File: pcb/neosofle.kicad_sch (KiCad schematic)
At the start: 69 parts, among them J1 JST_01x02_Socket, J2 JST_01x02_Pin, SW1 CPG135001S30, SW10 CPG135001S30, SW11 CPG135001S30, SW12 CPG135001S30, SW13 CPG135001S30, SW14 CPG135001S30, SW15 CPG135001S30, SW16 CPG135001S30, SW17 CPG135001S30, SW18 CPG135001S30, SW19 CPG135001S30, SW2 CPG135001S30, SW20 CPG135001S30, SW21 CPG135001S30, SW22 CPG135001S30, SW23 CPG135001S30, SW24 CPG135001S30, SW25 RotaryEncoder_Switch, SW26 CPG135001S30, SW27 CPG135001S30, SW28 CPG135001S30, SW29 CPG135001S30, SW3 CPG135001S30, SW30 CPG135001S30, SW4 CPG135001S30, SW5 CPG135001S30, SW6 CPG135001S30, SW7 CPG135001S30, SW8 CPG135001S30, SW9 CPG135001S30, U1 nice!nano v2

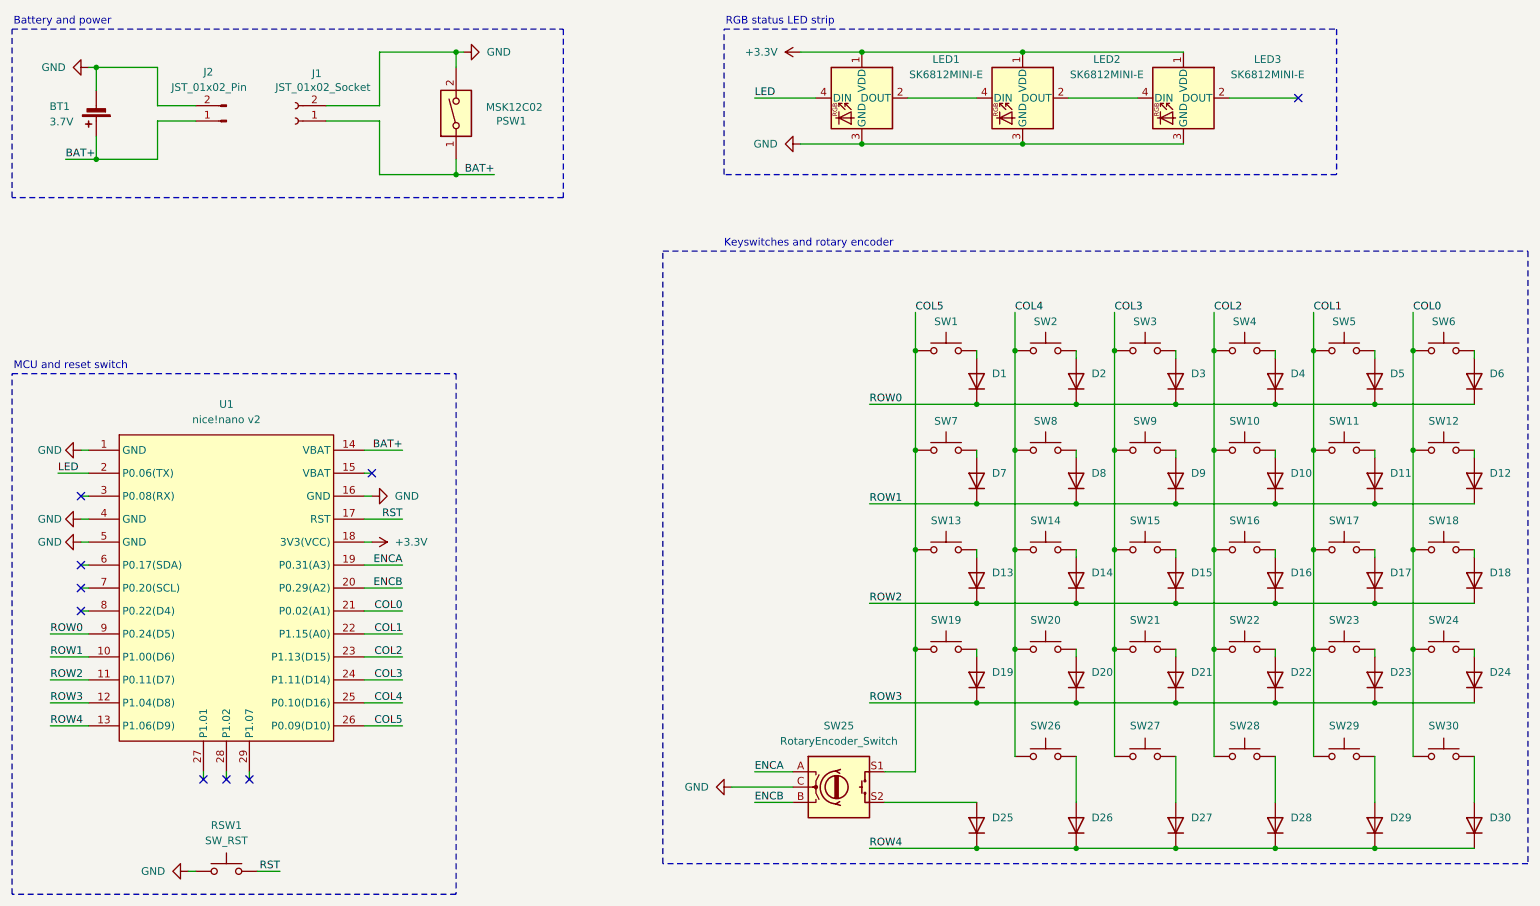
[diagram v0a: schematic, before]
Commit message: Correct battery and power net and their labels.
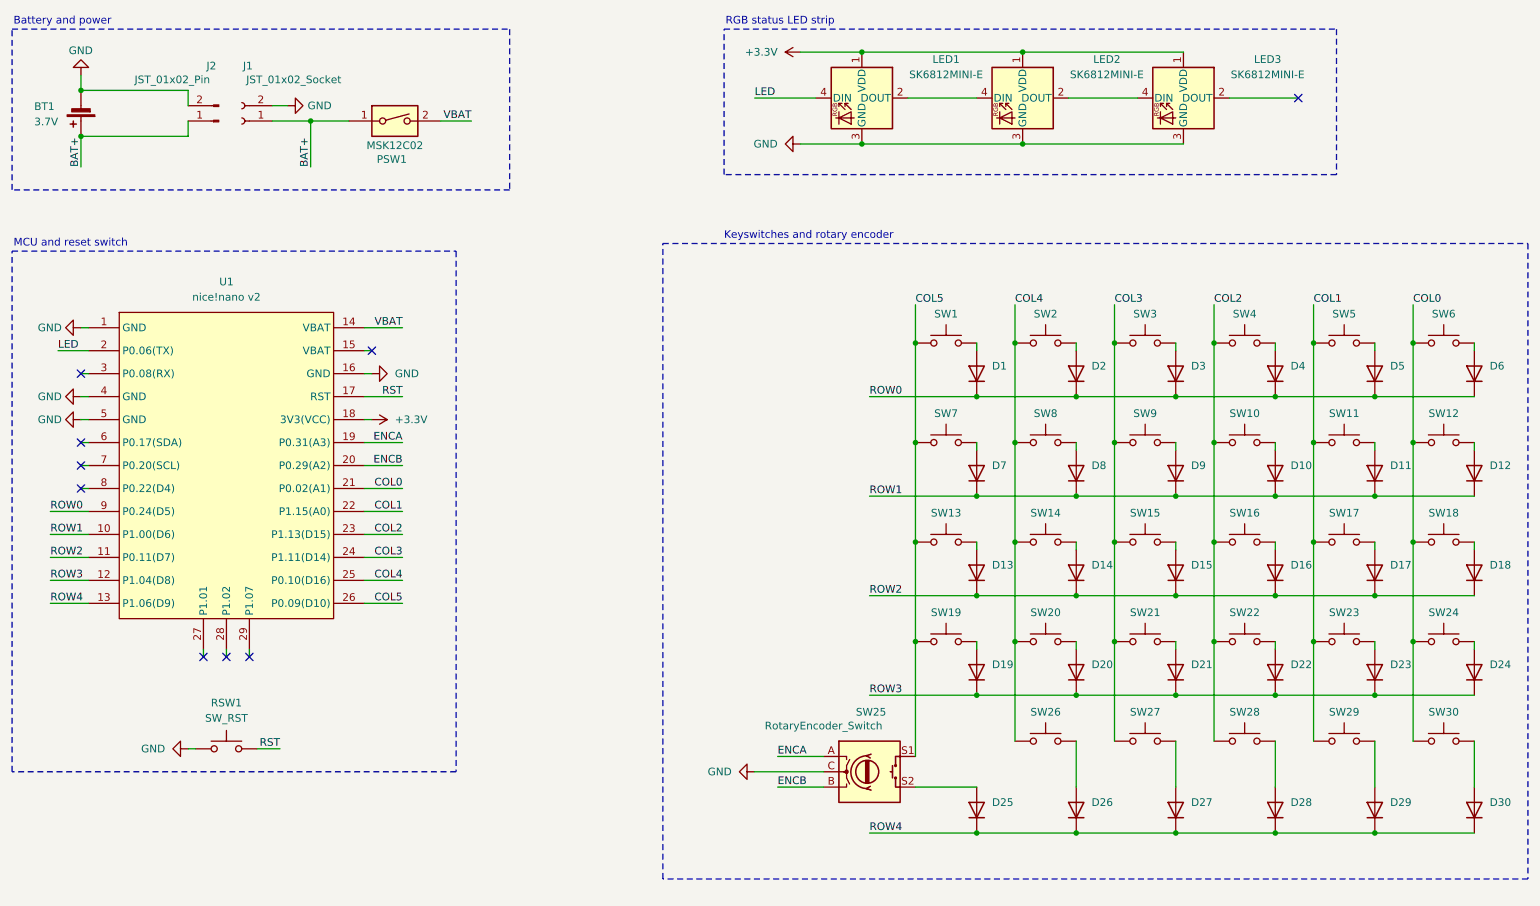
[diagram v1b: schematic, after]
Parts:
- LED1, LED2, LED3: footprint neosofle:SK6812MINI-E -> Custom_Keyboard:LED_SK6812MINI-E
- PSW1: footprint Custom_Keyboard:SW_Slide_SPDT_MSK12C02_HandSolder_Reversible -> Button_Switch_SMD:SW_SPDT_Shouhan_MSK12C02
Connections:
- net BAT+: no longer U1.14 (VBAT)
- net GND: no longer PSW1.2
- new net VBAT: PSW1.2, U1.14 (VBAT)
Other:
- moved on the sheet: BT1, D1, D10, D11, D12, D13, D14, D15, D16, D17, D18, D19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

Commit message: Add footprints, rename project to NeoSofle.
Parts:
- D1, D10, D11, D12, D13, D14, D15, D16, D17, D18, D19, D2, D20, D21, D22, D23, D24, D25, D26, D27, D28, D29, D3, D30, D4, D5, D6, D7, D8, D9: footprint Custom_Keyboard:D_SOD-123F_HandSolder_Reversible -> NeoSofle:D_SOD-123F_HandSolder
- J1: value JST_01x02_Socket -> JST_ACH_BM02B-ACHSS-GAN-ETF_Socket; footprint Custom_Keyboard:JST_ACH_BM02B-ACHSS-GAN-ETF_1x02-1MP_P1.20mm_Vertical_Reversible -> NeoSofle:JST_ACH_BM02B-ACHSS-GAN-ETF_1x02-1MP_P1.20mm_Vertical_HandSolder_Reversible
- J2: value JST_01x02_Pin -> JST_ACH_BM02B-ACHSS-GAN-ETF_Pin
- LED1, LED2, LED3: footprint Custom_Keyboard:LED_SK6812MINI-E -> NeoSofle:LED_SK6812MINI-E; symbol neosofle:SK6812MINI-E -> NeoSofle:SK6812MINI-E
- PSW1: footprint Button_Switch_SMD:SW_SPDT_Shouhan_MSK12C02 -> NeoSofle:SW_SPDT_MSK12C02_HandSolder
- RSW1: footprint Custom_Keyboard:SW_PUSH_1P1T_6x3.5mm_H4.3_APEM_MJTP1243_Reversible -> Button_Switch_THT:SW_PUSH_1P1T_6x3.5mm_H4.3_APEM_MJTP1243
- SW1, SW10, SW11, SW12, SW13, SW14, SW15, SW16, SW17, SW18, SW19, SW2, SW20, SW21, SW22, SW23, SW24, SW26, SW27, SW28, SW29, SW3, SW30, SW4, SW5, SW6, SW7, SW8, SW9: footprint Custom_Keyboard:SW_Choc_V2_HS_CPG135001S30_1u_Reversible -> NeoSofle:SW_Choc_V2_HS_CPG135001S30_1u
- SW25: footprint Custom_Keyboard:RotaryEncoder_Alps_EC11E-Switch_Vertical_H20mm_Reversible -> NeoSofle:RotaryEncoder_Bourns_PEC11L-Switch_Vertical15mm
- U1: footprint neosofle:nice_nano_Reversible -> NeoSofle:Nice_Nano_V2; symbol neosofle:nice_nano -> NeoSofle:nice_nano; now in the parts list

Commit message: Add 1u / 1.5u hybrid footprint for thumbkey, add teardrops, round tracks, add logo art and version text.
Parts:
- SW26: footprint NeoSofle:SW_Choc_V2_HS_CPG135001S30_1u -> NeoSofle:SW_Choc_V2_HS_CPG135001S30_1u1.5u_Hybrid
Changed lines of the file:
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@@
 			)
 		)
-		(property "Footprint" "NeoSofle:SW_Choc_V2_HS_CPG135001S30_1u"
+		(property "Footprint" "NeoSofle:SW_Choc_V2_HS_CPG135001S30_1u1.5u_Hybrid"
 			(at 194.31 132.08 0)
 			(effects

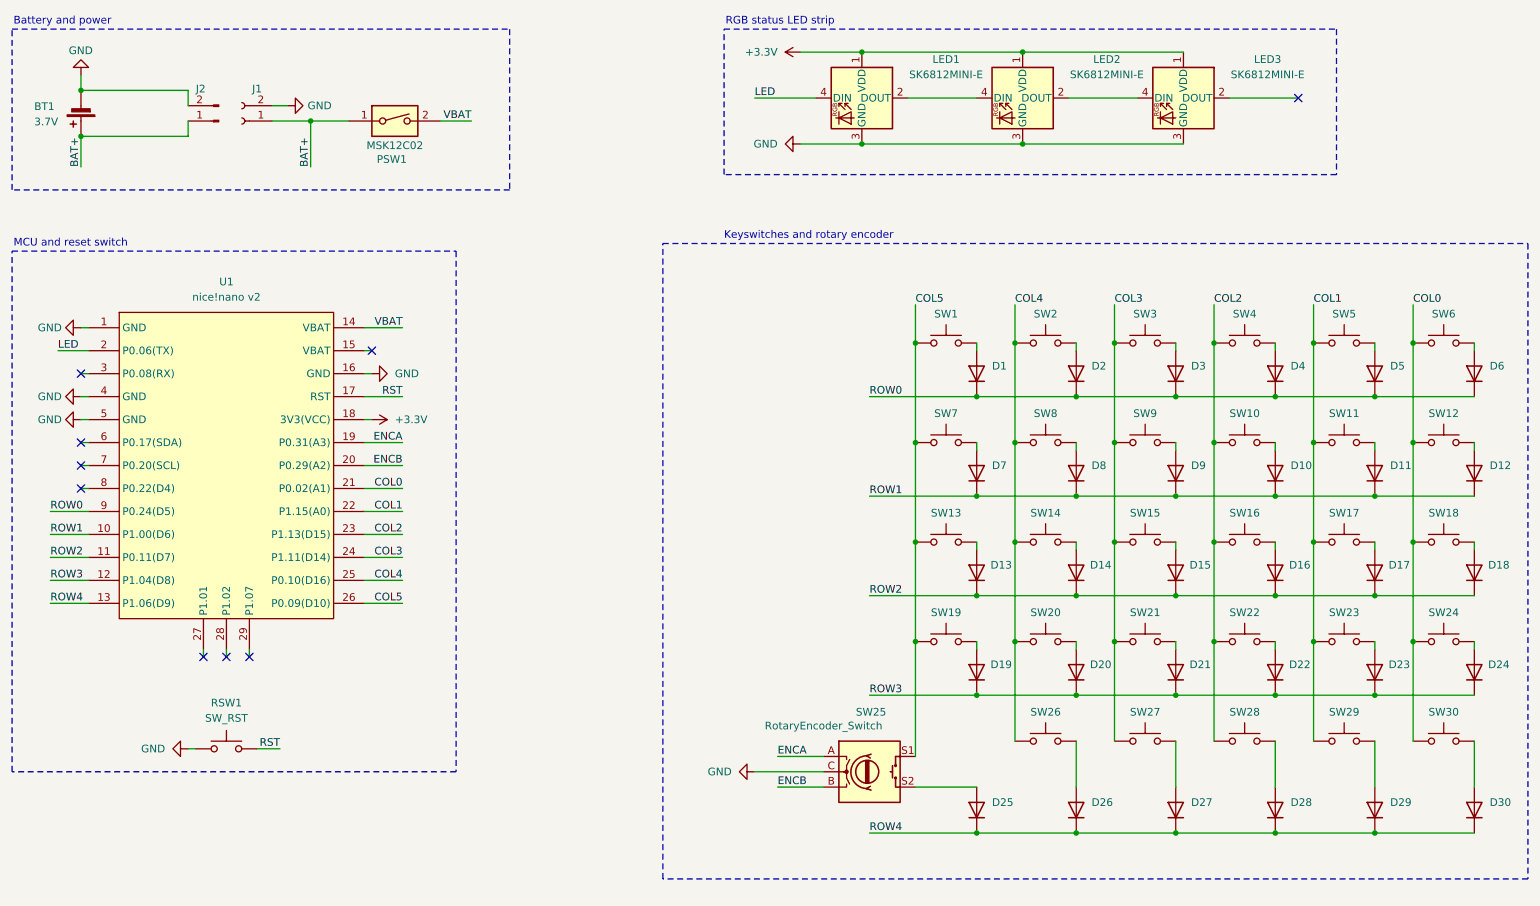
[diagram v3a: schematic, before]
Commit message: Update to hierarchical schematic reuse for both left and right half.
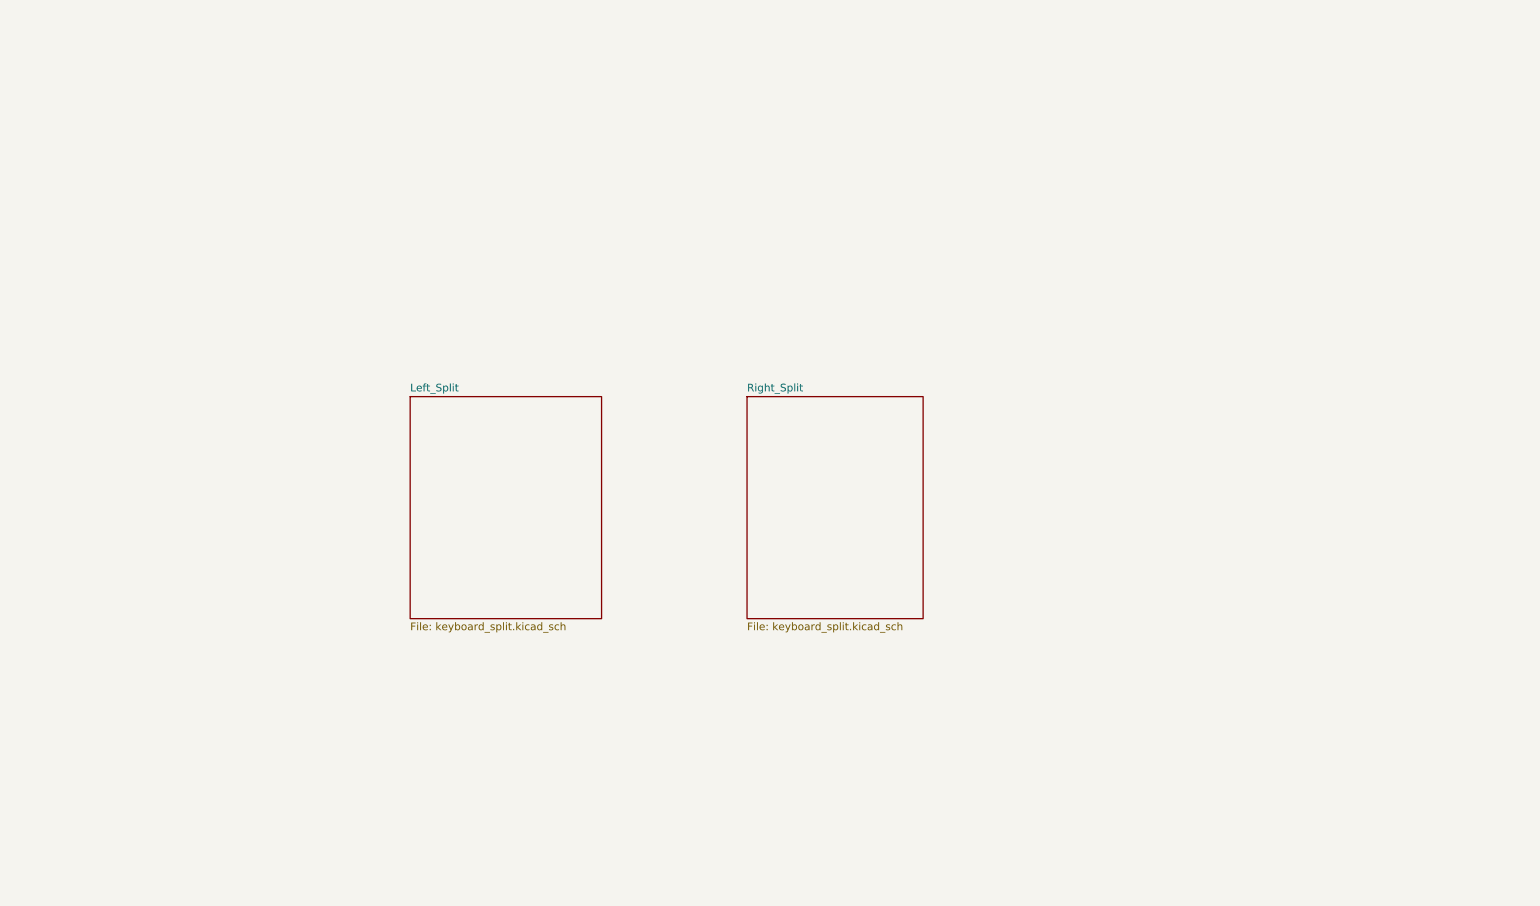
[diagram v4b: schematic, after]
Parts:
- removed BT1: 3.7V, symbol Device:Battery_Cell
- removed D1, D10, D11, D12, D13, D14, D15, D16, D17, D18, D19, D2, D20, D21, D22, D23, D24, D25, D26, D27, D28, D29, D3, D30, D4, D5, D6, D7, D8, D9: 1N4148W, NeoSofle:D_SOD-123F_HandSolder, symbol Diode:1N4148W
- removed J1: JST_ACH_BM02B-ACHSS-GAN-ETF_Socket, NeoSofle:JST_ACH_BM02B-ACHSS-GAN-ETF_1x02-1MP_P1.20mm_Vertical_HandSolder_Reversible, symbol Connector:Conn_01x02_Socket
- removed J2: JST_ACH_BM02B-ACHSS-GAN-ETF_Pin, symbol Connector:Conn_01x02_Pin
- removed LED1, LED2, LED3: SK6812MINI-E, NeoSofle:LED_SK6812MINI-E, symbol NeoSofle:SK6812MINI-E
- removed PSW1: MSK12C02, NeoSofle:SW_SPDT_MSK12C02_HandSolder, symbol Switch:SW_DIP_x01
- removed RSW1: SW_RST, Button_Switch_THT:SW_PUSH_1P1T_6x3.5mm_H4.3_APEM_MJTP1243, symbol Switch:SW_Push
- removed SW1, SW10, SW11, SW12, SW13, SW14, SW15, SW16, SW17, SW18, SW19, SW2, SW20, SW21, SW22, SW23, SW24, SW27, SW28, SW29, SW3, SW30, SW4, SW5, SW6, SW7, SW8, SW9: CPG135001S30, NeoSofle:SW_Choc_V2_HS_CPG135001S30_1u, symbol Switch:SW_Push
- removed SW25: RotaryEncoder_Switch, NeoSofle:RotaryEncoder_Bourns_PEC11L-Switch_Vertical15mm, symbol Device:RotaryEncoder_Switch
- removed SW26: CPG135001S30, NeoSofle:SW_Choc_V2_HS_CPG135001S30_1u1.5u_Hybrid, symbol Switch:SW_Push
- removed U1: nice!nano v2, NeoSofle:Nice_Nano_V2, symbol NeoSofle:nice_nano
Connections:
- no-connect marks 9 -> 0
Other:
- added sheet Left_Split (keyboard_split.kicad_sch)
- added sheet Right_Split (keyboard_split.kicad_sch)
- note removed: "Battery and power"
- note removed: "Keyswitches and rotary encoder"
- note removed: "MCU and reset switch"
- note removed: "RGB status LED strip"
